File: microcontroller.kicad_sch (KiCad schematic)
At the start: 18 parts, among them J901 SWD_Conn, U901 STM32F103RBTx, Y901 8MHz

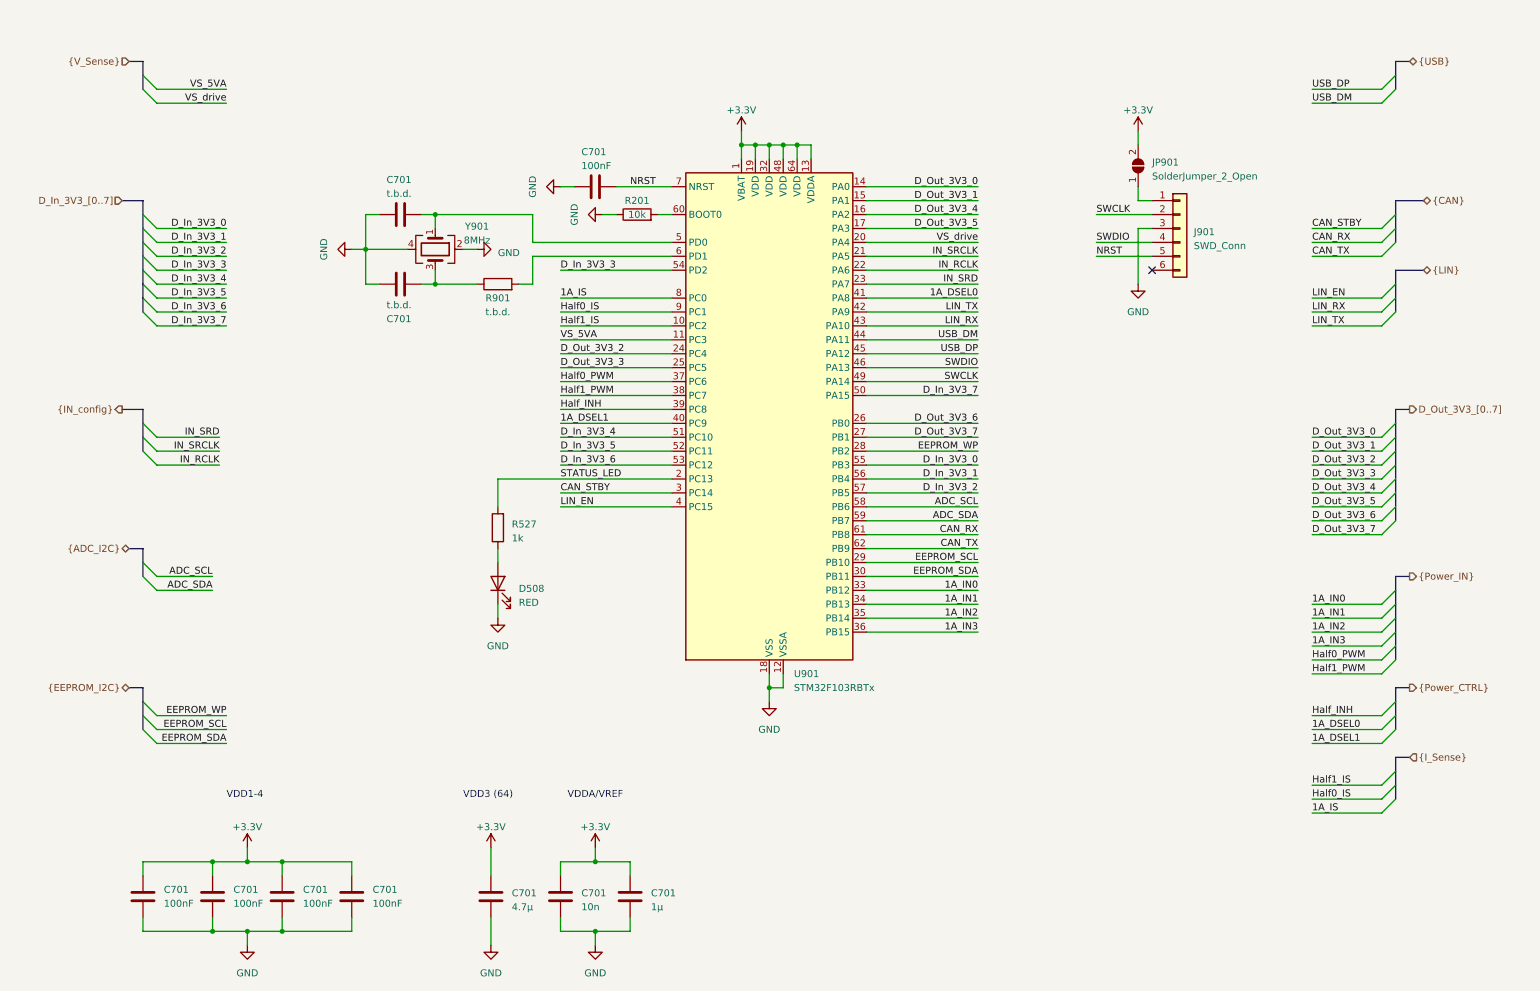
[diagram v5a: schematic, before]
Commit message: hierarchical sheets for digital I/O and replaced power supply jumpers with relays
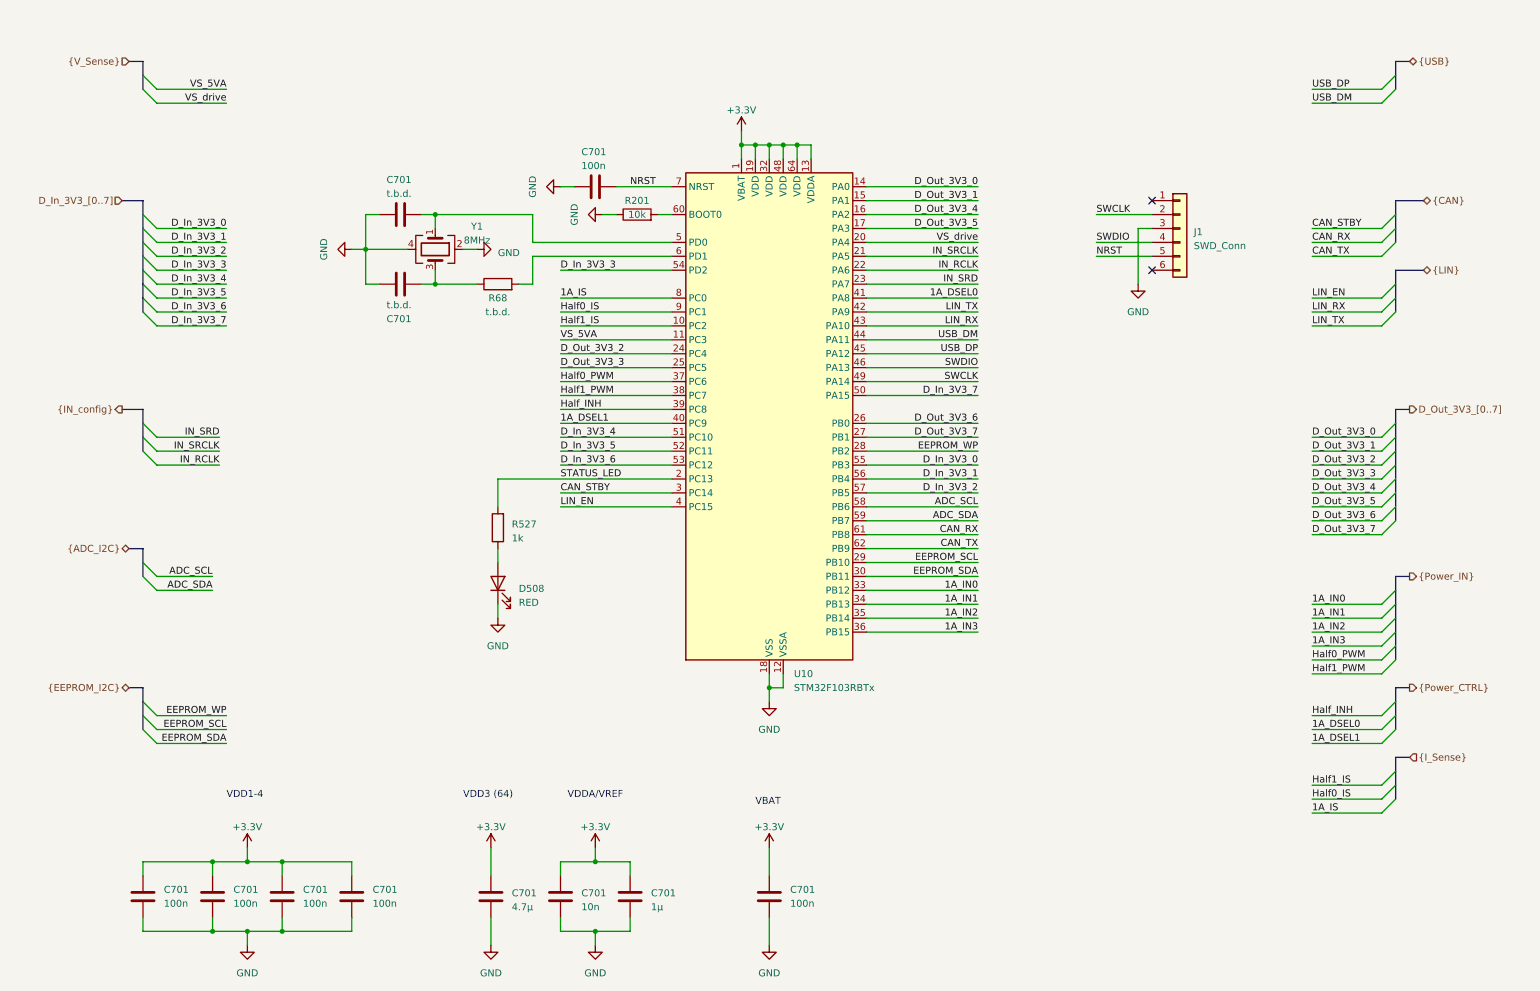
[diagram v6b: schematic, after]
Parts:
- removed JP901: SolderJumper_2_Open, Jumper:SolderJumper-2_P1.3mm_Open_Pad1.0x1.5mm, symbol Jumper:SolderJumper_2_Open
- added C701: 100n, Capacitor_SMD:C_0603_1608Metric, symbol Device:C
- C701: value 100nF -> 100n
- renumbered J901 to J1, R901 to R68, U901 to U10, Y901 to Y1
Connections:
- net +3.3V: now also C701.1
- net GND: now also C701.2
- no-connect marks 1 -> 2
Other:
- note added: "VBAT"

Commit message: added missing values and possible improvements
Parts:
- C701: value t.b.d. -> 10p
- R68: value t.b.d. -> 0
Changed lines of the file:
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@@
 (kicad_sch (version 20230121) (generator eeschema)
   (paper "A4")
+  (bus_alias "V_Sense" (members "VS_5VA" "VS_drive" ""))
   (bus_alias "ADC_I2C" (members "ADC_SCL" "ADC_SDA"))
+  (bus_alias "USB" (members "USB_DP" "USB_DM"))
+  (bus_alias "IN_config" (members "IN_SRD" "IN_SRCLK" "IN_RCLK" "IN_SRD_AIn"))
   (bus_alias "EEPROM_I2C" (members "EEPROM_SCL" "EEPROM_SDA" "EEPROM_WP"))
-  (bus_alias "V_Sense" (members "VS_5VA" "VS_drive" ""))
-  (bus_alias "IN_config" (members "IN_SRD" "IN_SRCLK" "IN_RCLK" "IN_SRD_AIn"))
-  (bus_alias "USB" (members "USB_DP" "USB_DM"))
   (junction (at 157.48 40.64) (diameter 0) (color 0 0 0 0)
   )
@@
       (effects (font (size 1.27 1.27)))
     )
-    (property "Value" "t.b.d." (at 102.87 71.12 90)
+    (property "Value" "0" (at 102.87 71.12 90)
       (effects (font (size 1.27 1.27)))
     )
@@
       (effects (font (size 1.27 1.27)) (justify left))
     )
-    (property "Value" "t.b.d." (at 82.55 49.53 90)
+    (property "Value" "10p" (at 82.55 49.53 90)
       (effects (font (size 1.27 1.27)) (justify left))
     )
@@
       (effects (font (size 1.27 1.27)) (justify left))
     )
-    (property "Value" "t.b.d." (at 82.55 69.85 90)
+    (property "Value" "10p" (at 82.55 69.85 90)
       (effects (font (size 1.27 1.27)) (justify left))
     )
